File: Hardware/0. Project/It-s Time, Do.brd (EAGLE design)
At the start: 160 x 100 mm, 67 parts, among them CN1 CELL-CONNECTOR, CN13 USB 3.2 Gen 2 Type C Receptac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, CN2 2P-MINI-FIT-JR, CN3 3P-MINI-FIT-JR, CN4 JTAG, CN5 CR-1220, Q1 P-FET-ENHANCEMENT-SI2369BDS, Q14 NPN-BC817, Q15 NPN-BC817, Q3 BC817, U1 MCP73831, U12 CP2102N, U2 TLV75530PDBVR, U3 LMV321, U8 DS3231-SO16

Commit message: Schematic WIP
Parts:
- removed C75, C76: 1nF, My-RLC:C0603
- removed R78: DNP, My-RLC:R0603
- added C11, C12: 1nF, My-RLC:C0603
- R76, R77: value 22R -> 22R (5%)
- R82: value 22k -> 10k (5%)
- R83, R85: value 4k7 -> 4k7 (5%)
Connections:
- net ADC_BATTERY_VOLTAGE renamed ESP32_ADC_BATTERY_SUPPLY_MONITOR
- net GPIO_BATTERY_CHARGING_STATUS renamed ESP32_GPIO_BATTERY_CHARGING_STATUS
- removed net ESP32_GPIO_USB_DETECT: R71.2, R72.1
- removed net ESP32_GPIO_USB_DETECT1: U12.8
- removed net ESP32_PROG_ENABLE: C44.1, C75.1, CN4.10, Q14.3, R86.2, SOC1.3
- removed net ESP32_PROG_MODE: C76.1, Q15.3, R87.2, SOC1.25
- removed net ESP32_SERIAL1_UART_RX: SOC1.27
- removed net ESP32_SERIAL1_UART_TX: SOC1.28
- removed net ESP32_SERIAL2_UART_RX: SOC1.7
- removed net ESP32_SERIAL2_UART_TX: SOC1.9
- removed net ESP32_SERIAL_UART_RX: SOC1.34
- removed net ESP32_SERIAL_UART_TX: SOC1.35
- removed net N$48: R82.1, U12.9
- removed net N$49: R78.2, U12.11
- new net ESP32_GPIO_EXTERNAL_SUPPLY_MONITOR: R71.2, R72.1, U12.8
- new net ESP32_GPIO_PROG_ENABLE: C11.1, C44.1, CN4.10, Q14.3, R86.2, SOC1.3
- new net ESP32_GPIO_PROG_MODE: C12.1, Q15.3, R87.2, SOC1.25
- new net N$17: C72.2, U12.3, U12.EXP, U12.M
- new net N$18: R82.2, U12.9
- net 0V: now also C11.2, C12.2; no longer C72.2, C75.2, C76.2, R78.1, U12.3, U12.EXP, U12.M
- net 3.3V: now also R82.1; no longer R82.2
- net ESP32_UART_RX_USB: now also SOC1.34
- net ESP32_UART_TX_USB: now also SOC1.35
- net ESP32_USB_RTS: now also R85.1; no longer R85.2
- net N$16: now also R85.2; no longer R85.1

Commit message: Schematic WIP
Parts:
- removed C46: 100nF, My-RLC:C0603
- removed Q14: NPN-BC817, My-Transistors:SOT23-3
- removed R71: 24k, My-RLC:R0603
- removed R86, R87: 10k (1%), My-RLC:R0603
- removed U8: DS3231-SO16, My-ICs:SOIC-16W_(SO16)
- added C14: 1nF, My-RLC:C0603
- added C16: 10nF, My-RLC:C0603
- added Q4: BC817, My-Transistors:SOT23-3
- added R14: 47R, My-RLC:R0603
- added R20: 4k7 (5%), My-RLC:R0603
- added R21: 10k (5%), My-RLC:R0603
- added U4: LMV321, My-OpAmps:SOT-23-5
- C10: value 100nF -> 100uF x 10V; device My-RLC:C0603 -> My-RLC:PTH-5MM
- C12: value 1nF -> 100nF
- C2: value 10nF -> 1uF
- C3: value 100nF -> 10uF
- C6: value 10uF -> 100nF
- C7: value 100uF x 10V -> 100nF; device My-RLC:PTH-5MM -> My-RLC:C0603
- C8: value 1uF -> 10uF
- CN1: value CELL-CONNECTOR -> CR-1220; device My-Battery:JST-PH2 -> My-Battery:CR1220/1225_HOLDER
- CN2: value 2P-MINI-FIT-JR -> CELL-CONNECTOR; device My-Connectors:MINI-FIT-JR-2P -> My-Battery:JST-PH2
- CN3: value 3P-MINI-FIT-JR -> JTAG; device My-Connectors:MINI-FIT-JR-3P -> My-Connectors:JTAG-ARM-10P
- CN4: value JTAG -> 2P-MINI-FIT-JR; device My-Connectors:JTAG-ARM-10P -> My-Connectors:MINI-FIT-JR-2P
- CN5: value CR-1220 -> 3P-MINI-FIT-JR; device My-Battery:CR1220/1225_HOLDER -> My-Connectors:MINI-FIT-JR-3P
- Q3: value BC817 -> NPN-BC817
- R1: value 47R -> 10k (5%)
- R11: value 4k7 (5%) -> 24k
- R13: value 10k (5%) -> 22K (5%)
- R15, R16: value 1M -> 10k (1%)
- R2, R3: value 4k7 (5%) -> 10k (5%)
- R5, R6: value 10k (5%) -> 4k7 (5%)
- R7: value 10k (5%) -> 100R (5%)
- R8: value 4k7 -> 1M
- R9: value 100R (5%) -> 1M
- U1: value MCP73831 -> DS3231-SO16; device My-ICs:SOT-23-5 -> My-ICs:SOIC-16W_(SO16)
- U3: value LMV321 -> MCP73831; device My-OpAmps:SOT-23-5 -> My-ICs:SOT-23-5
- moved C4 232.2 mm to (-98.1, -129.9)
- moved R15 221.1 mm to (-77.9, -121.1)
- moved R16 211.3 mm to (-68.7, -113.8)
- moved C12 210.4 mm to (-77.5, 80.0)
- moved R13 154.5 mm to (-22.9, 94.0)
- moved CN3 154.3 mm to (-54.6, 57.1)
- moved CN5 147.0 mm to (-71.9, -96.2)
- moved R11 134.8 mm to (-57.1, 94.0)
- moved Q3 65.0 mm to (-73.2, -106.8)
- moved CN2 58.4 mm to (-43.2, 69.8)
- moved R1 56.2 mm to (-74.9, 87.6)
- moved CN4 47.5 mm to (-41.9, 11.4)
- moved CN1 35.3 mm to (-21.6, 41.9)
- moved U1 34.9 mm to (-44.5, 58.4)
- moved C3 33.0 mm to (-25.4, 88.9)
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- renumbered C44 to C15, C45 to C13, C67 to C20, C69 to C19, C71 to C18, C72 to C21, CN13 to CN6, D7 to D2, Q15 to Q2, R62 to R24, R63 to R23, R65 to R18, R72 to R12, R76 to R25, R77 to R26, R82 to R22, R83 to R19, R85 to R17, U12 to U5
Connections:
- net ESP32_USB_DTR renamed N$20
- removed net N$17: C21.2, U5.3, U5.EXP, U5.M
- removed net N$9: CN5.+, U8.14
- new net RTC_VBAT: C4.1, CN1.+, U1.14
- net !DISPLAY_OLED_RESET: now also R2.1; no longer R5.1
- net 0V: now also C14.2, C16.2, C17.2, C21.2, C7.1, CN1.-, CN3.3, CN3.5, CN3.9, CN4.2, Q4.2, R13.1, R21.2, R3.1, R9.1, U1.10, U1.11, U1.12, U1.13, U1.5, U1.6, U1.7, U1.8, U1.9, U4.2, U5.3, U5.EXP, U5.M; no longer C17.1, C46.2, C7.2, CN1.2, CN4.3, CN4.5, CN4.9, CN5.-, Q3.2, R13.2, R16.1, R7.1, R8.1, U1.2, U8.10, U8.11, U8.12, U8.13, U8.5, U8.6, U8.7, U8.8, U8.9
- net 3.3V: now also C12.1, C17.1, C2.1, C7.2, CN3.1, R1.2, R15.1, R16.1, U1.2, U4.5; no longer C10.1, C17.2, C4.1, C46.1, CN4.1, R3.2, R86.1, R87.1, U3.5, U8.2
- net ESP32_ADC_BATTERY_SUPPLY_MONITOR: now also R8.1, R9.2, SOC1.4; no longer R15.1, R16.2
- net ESP32_ADC_TASK_FEEDBACK_MONITOR: now also C16.1, R14.2; no longer C2.1, R1.2
- net ESP32_GPIO_BATTERY_CHARGING_STATUS: now also SOC1.6, U3.1; no longer U1.1
- net ESP32_GPIO_EXTERNAL_SUPPLY_MONITOR: now also R11.2, SOC1.5; no longer R71.2
- net ESP32_GPIO_PROG_ENABLE: now also C14.1, CN3.10, Q3.3, R16.2; no longer C11.1, CN4.10, Q14.3, R86.2
- net ESP32_GPIO_PROG_MODE: now also C11.1, R15.2; no longer C12.1, R87.2
- net ESP32_GPIO_TASK_CONTROLLER: now also R20.2, R21.1; no longer R11.2, R13.1
- net ESP32_I2C_SCL: now also R5.1, U1.16; no longer R3.1, U8.16
- net ESP32_I2C_SDA: now also R6.1, U1.15; no longer R2.1, U8.15
- net ESP32_USB_RTS: now also Q3.2; no longer Q14.2
- net JTAG_TCK: now also CN3.4; no longer CN4.4
- net JTAG_TDI: now also CN3.8; no longer CN4.8
- net JTAG_TDO: now also CN3.6; no longer CN4.6
- net JTAG_TMS: now also CN3.2; no longer CN4.2
- net N$1: now also C3.1; no longer C5.1
- net N$11: now also R7.2; no longer R9.2
- net N$12: now also R14.1, U4.1, U4.4; no longer R1.1, U3.1, U3.4
- net N$13: now also Q3.1; no longer Q14.1
- net N$14: now also CN5.2; no longer CN3.2
- net N$15: now also CN5.3; no longer CN3.3
- net N$2: now also R1.1; no longer R6.1
- net N$26: now also R13.2, U3.5; no longer R8.2, U1.5
- net N$3: now also R3.2; no longer R7.2
- net N$4: now also CN4.1, U4.3; no longer CN2.1, U3.3
- net N$41: now also Q4.1, R20.1; no longer Q3.1, R11.1
- net N$42: now also Q4.3; no longer Q3.3
- net N$5: now also CN5.1; no longer CN3.1
- net N$7: now also C5.1; no longer C6.1
- net P$1: now also CN2.1, R8.2, U3.3; no longer CN1.1, R15.2, U1.3
- net USB_N: now also CN6.A7, CN6.B7
- net USB_P: now also CN6.A6, CN6.B6
- net VBUS: now also R11.1, R7.1, U3.4; no longer R71.1, R9.1, U1.4
- net VSYS: now also C10.1, C6.1; no longer C3.1, C7.1

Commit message: Schematic WIP
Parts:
- C10: value 100uF x 10V -> 100nF; device My-RLC:PTH-5MM -> My-RLC:C0603
- C12: value 100nF -> 100uF x 10V; device My-RLC:C0603 -> My-RLC:PTH-5MM
- C13, C15, C3, C5: value 10uF -> 100nF
- C14: value 1nF -> 10uF
- C16: value 10nF -> 100nF
- C17, C19, C7, C9: value 100nF -> 10uF
- C2: value 1uF -> 4.7nF
- C20: value 4.7nF -> 1uF
- C6: value 100nF -> 10nF
- C8: value 10uF -> 1nF
- CN1: value CR-1220 -> USB 3.2 Gen 2 Type C Receptacle; device My-Battery:CR1220/1225_HOLDER -> My-Connectors:USB-C-24P
- CN2: value CELL-CONNECTOR -> 3P-MINI-FIT-JR; device My-Battery:JST-PH2 -> My-Connectors:MINI-FIT-JR-3P
- CN3: value JTAG -> 2P-MINI-FIT-JR; device My-Connectors:JTAG-ARM-10P -> My-Connectors:MINI-FIT-JR-2P
- CN4: value 2P-MINI-FIT-JR -> JTAG; device My-Connectors:MINI-FIT-JR-2P -> My-Connectors:JTAG-ARM-10P
- CN5: value 3P-MINI-FIT-JR -> CELL-CONNECTOR; device My-Connectors:MINI-FIT-JR-3P -> My-Battery:JST-PH2
- CN6: value USB 3.2 Gen 2 Type C Receptacle -> CR-1220; device My-Connectors:USB-C-24P -> My-Battery:CR1220/1225_HOLDER
- D1: value SCHOTTKY-SS16 -> FM4004
- D2: value FM4004 -> SCHOTTKY-SS16
- Q1: value P-FET-ENHANCEMENT-SI2369BDS -> BC817
- Q4: value BC817 -> P-FET-ENHANCEMENT-SI2369BDS
- R1, R2: value 10k (5%) -> 22R (5%)
- R10: value 10k (5%) -> 10k (1%)
- R11: value 24k -> 4k7 (5%)
- R12: value 47k -> 10k (1%)
- R13: value 22K (5%) -> 47R
- R14: value 47R -> 22K (5%)
- R15: value 10k (1%) -> 24k
- R16: value 10k (1%) -> 47k
- R17, R5, R6: value 4k7 (5%) -> 10k (5%)
- R18: value 5k1 -> 1M
- R19: value 4k7 (5%) -> 1M
- R20: value 4k7 (5%) -> 100R (5%)
- R21, R22: value 10k (5%) -> 4k7 (5%)
- R23: value 1M -> 390k (1%)
- R24: value 5k1 -> 10k (5%)
- R25, R26: value 22R (5%) -> 10k (5%)
- R3: value 10k (5%) -> 5k1
- R4: value 390k (1%) -> 1M
- R7: value 100R (5%) -> 4k7 (5%)
- R8: value 1M -> 4k7 (5%)
- R9: value 1M -> 5k1
- U1: value DS3231-SO16 -> CP2102N; device My-ICs:SOIC-16W_(SO16) -> My-ICs:QFN-28
- U2: value TLV75530PDBVR -> LMV321; device My-LDOs:SOT-23-5 -> My-OpAmps:SOT-23-5
- U4: value LMV321 -> TLV75530PDBVR; device My-OpAmps:SOT-23-5 -> My-LDOs:SOT-23-5
- U5: value CP2102N -> DS3231-SO16; device My-ICs:QFN-28 -> My-ICs:SOIC-16W_(SO16)
- moved R17 231.8 mm to (-15.2, 94.0)
- moved C18 230.8 mm to (-98.1, -129.9)
- moved C4 230.8 mm to (-41.9, 94.0)
- moved R8 230.2 mm to (-75.6, -131.0)
- moved R19 229.4 mm to (-30.5, 94.0)
- moved C14 228.8 mm to (-20.3, 88.9)
- moved C8 228.8 mm to (-87.3, -129.9)
- moved R11 225.4 mm to (-71.3, -131.0)
- moved R22 219.1 mm to (-64.8, 87.6)
- moved R5 219.1 mm to (-79.9, -131.0)
- moved R15 216.1 mm to (-57.1, 94.0)
- moved R12 215.8 mm to (-77.9, -121.1)
- moved R10 214.6 mm to (-68.7, -113.8)
- moved R25 213.9 mm to (-80.0, 87.6)
- moved R26 213.8 mm to (-74.9, 87.6)
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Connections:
- net !DISPLAY_OLED_RESET: now also R24.1; no longer R2.1
- net 0V: now also C15.1, C18.2, C19.2, C2.1, C20.2, C3.1, C4.1, C7.2, CN1.A1, CN1.A12, CN1.B1, CN1.B12, CN3.2, CN4.3, CN4.5, CN4.9, CN5.2, CN6.-, Q1.2, R14.1, R16.2, R17.1, R19.1, R23.1, R25.1, R3.2, R4.2, R6.2, R9.2, U1.3, U1.EXP, U1.M, U5.10, U5.11, U5.12, U5.13, U5.5, U5.6, U5.7, U5.8, U5.9; no longer C15.2, C18.1, C19.1, C2.2, C20.1, C3.2, C4.2, C7.1, CN1.-, CN2.2, CN3.3, CN3.5, CN3.9, CN4.2, CN6.A1, CN6.A12, CN6.B1, CN6.B12, Q4.2, R10.1, R12.2, R13.1, R18.2, R21.2, R23.2, R24.2, R3.1, R4.1, R9.1, U1.10, U1.11, U1.12, U1.13, U1.5, U1.6, U1.7, U1.8, U1.9, U5.3, U5.EXP, U5.M
- net 3.3V: now also C10.1, C14.1, C15.2, C20.1, C5.1, CN4.1, R10.1, R12.1, R21.2, R22.2, R24.2, R26.2, R5.1, U1.6, U1.7, U5.2; no longer C12.1, C17.1, C2.1, C7.2, C8.1, CN3.1, R1.2, R15.1, R16.1, R2.2, R22.1, R5.2, R6.2, U1.2, U5.6, U5.7
- net ESP32_ADC_BATTERY_SUPPLY_MONITOR: now also R18.1, R19.2; no longer R8.1, R9.2
- net ESP32_ADC_TASK_FEEDBACK_MONITOR: now also C6.1, R13.2, SOC1.11; no longer C16.1, R14.2
- net ESP32_GPIO_EXTERNAL_SUPPLY_MONITOR: now also R15.2, R16.1, U1.8; no longer R11.2, R12.1, U5.8
- net ESP32_GPIO_PROG_ENABLE: now also C7.1, C8.1, CN4.10, Q2.3, R10.2; no longer C14.1, C15.1, CN3.10, Q3.3, R16.2
- net ESP32_GPIO_PROG_MODE: now also Q3.3, R12.2; no longer Q2.3, R15.2
- net ESP32_GPIO_TASK_CONTROLLER: now also R6.1, R7.2, SOC1.8; no longer R20.2, R21.1
- net ESP32_I2C_SCL: now also R22.1, U5.16; no longer R5.1, U1.16
- net ESP32_I2C_SDA: now also R21.1, U5.15; no longer R6.1, U1.15
- net ESP32_UART_RX_USB: now also U1.26; no longer U5.26
- net ESP32_UART_TX_USB: now also U1.25; no longer U5.25
- net ESP32_USB_RTS: now also Q2.2, R11.1, U1.24; no longer Q3.2, R17.1, U5.24
- net JTAG_TCK: now also CN4.4; no longer CN3.4
- net JTAG_TDI: now also CN4.8; no longer CN3.8
- net JTAG_TDO: now also CN4.6; no longer CN3.6
- net JTAG_TMS: now also CN4.2; no longer CN3.2
- net N$1: now also C19.1; no longer C3.1
- net N$10: now also C2.2, CN1.G1, CN1.G2, CN1.G3, CN1.G4, R4.1; no longer C20.2, CN6.G1, CN6.G2, CN6.G3, CN6.G4, R23.1
- net N$11: now also Q4.1, R20.2; no longer Q1.1, R7.2
- net N$12: now also R13.1, U2.1, U2.4; no longer R14.1, U4.1, U4.4
- net N$13: now also Q2.1, R8.1; no longer Q3.1, R19.1
- net N$14: now also CN2.2; no longer CN5.2
- net N$15: now also CN2.3; no longer CN5.3
- net N$16: now also Q3.1, R11.2; no longer Q2.1, R17.2
- net N$18: now also R5.2, U1.9; no longer R22.2, U5.9
- net N$19: now also R1.2, U1.5; no longer R25.2, U5.5
- net N$2: now also R26.1; no longer R1.1
- net N$20: now also Q3.2, R8.2, U1.28; no longer Q2.2, R19.2, U5.28
- net N$21: now also CN1.B5, R9.1; no longer CN6.B5, R18.1
- net N$22: now also R2.2, U1.4; no longer R26.2, U5.4
- net N$26: now also R14.2; no longer R13.2
- net N$3: now also R25.2; no longer R3.2
- net N$4: now also CN3.1, U2.3; no longer CN4.1, U4.3
- net N$41: now also Q1.1, R7.1; no longer Q4.1, R20.1
- net N$42: now also D1.2, Q1.3; no longer D2.2, Q4.3
- net N$5: now also CN2.1; no longer CN5.1
- net N$6: now also R23.2; no longer R4.2
- net N$7: now also C17.1; no longer C5.1
- net N$8: now also CN1.A5, R3.1; no longer CN6.A5, R24.1
- net P$1: now also CN5.1, Q4.3, R18.2; no longer CN2.1, Q1.3, R8.2
- net RTC_VBAT: now also C18.1, CN6.+, U5.14; no longer C4.1, CN1.+, U1.14
- net USB_N: now also CN1.A7, CN1.B7, R1.1; no longer CN6.A7, CN6.B7, R25.1
- net USB_P: now also CN1.A6, CN1.B6, R2.1; no longer CN6.A6, CN6.B6, R26.1
- net VBUS: now also C3.2, C4.2, CN1.A4, CN1.A9, CN1.B4, CN1.B9, D1.1, D2.2, R15.1, R17.2, R20.1; no longer C18.2, C19.2, CN6.A4, CN6.A9, CN6.B4, CN6.B9, D1.2, D2.1, R10.2, R11.1, R7.1
- net VSYS: now also C12.1, C16.1, D2.1, Q4.2, U4.1, U4.3; no longer C10.1, C6.1, D1.1, Q1.2, U2.1, U2.3

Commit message: Schematic v1.0 release
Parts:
- R13: value 47R -> 47R (5%)
- R15: value 24k -> 24k (5%)
- R16: value 47k -> 47k (5%)
- R18, R19, R4: value 1M -> 1M (1%)
- R3, R9: value 5k1 -> 5k1 (1%)
- moved C1 136.6 mm to (-97.5, 12.9)
- moved CN2 136.6 mm to (-98.6, 37.8)
- moved D1 136.6 mm to (-104.1, 90.8)
- moved K1 136.6 mm to (-101.3, 50.5)
- moved Q1 136.6 mm to (-97.8, 92.1)
- moved Q2 136.6 mm to (-99.9, 27.1)
- moved Q3 136.6 mm to (-105.9, 19.1)
- moved R1 136.6 mm to (-97.9, 7.94)
- moved R10 136.6 mm to (-95.4, 20.2)
- moved R11 136.6 mm to (-97.9, 3.02)
- moved R12 136.6 mm to (-104.6, 12.9)
- moved R2 136.6 mm to (-93.7, 7.94)
- moved R5 136.6 mm to (-106.5, 3.02)
- moved R6 136.6 mm to (-106.7, 84.5)
- moved R7 136.6 mm to (-91.4, 93.3)
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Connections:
- net 0V: now also C5.1; no longer C5.2
- net 3.3V: now also C5.2; no longer C5.1

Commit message: Board design WIP
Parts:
- moved C18 224.8 mm to (99.5, 19.1), flipped to the bottom
- moved C11 214.0 mm to (94.1, 19.1), flipped to the bottom
- moved C8 203.3 mm to (88.7, 19.1), flipped to the bottom
- moved R5 188.4 mm to (81.3, 17.9), flipped to the bottom
- moved Q3 187.1 mm to (80.6, 34.0), flipped to the bottom
- moved R12 184.6 mm to (79.4, 27.8), flipped to the bottom
- moved R6 181.2 mm to (74.5, 79.9), flipped to the bottom
- moved R8 179.8 mm to (77.0, 17.9), flipped to the bottom
- moved D1 176.1 mm to (71.9, 86.2), flipped to the bottom
- moved Q2 175.1 mm to (74.6, 42.1), flipped to the bottom
- moved R1 171.3 mm to (72.7, 22.9), flipped to the bottom
- moved R11 171.3 mm to (72.7, 17.9), flipped to the bottom
- moved C1 170.4 mm to (72.2, 27.8), flipped to the bottom
- moved R10 166.2 mm to (70.2, 35.1), flipped to the bottom
- moved Q1 163.4 mm to (65.6, 87.5), flipped to the bottom
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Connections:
- net 0V: now also C2.2, R4.1; no longer C2.1, R4.2
- net N$10: now also C2.1, R4.2; no longer C2.2, R4.1
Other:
- board size 160 x 100 mm -> 50 x 50 mm

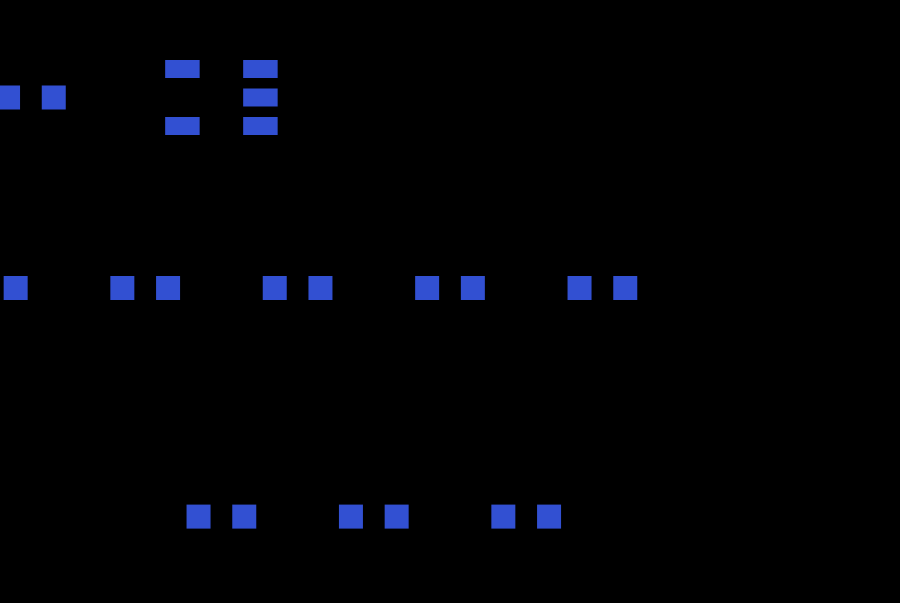
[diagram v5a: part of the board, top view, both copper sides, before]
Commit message: Schematic v1.1 release
- Minor improvements on parts designators position;
- Just one resistor as pull up in not used pins at OLED display.
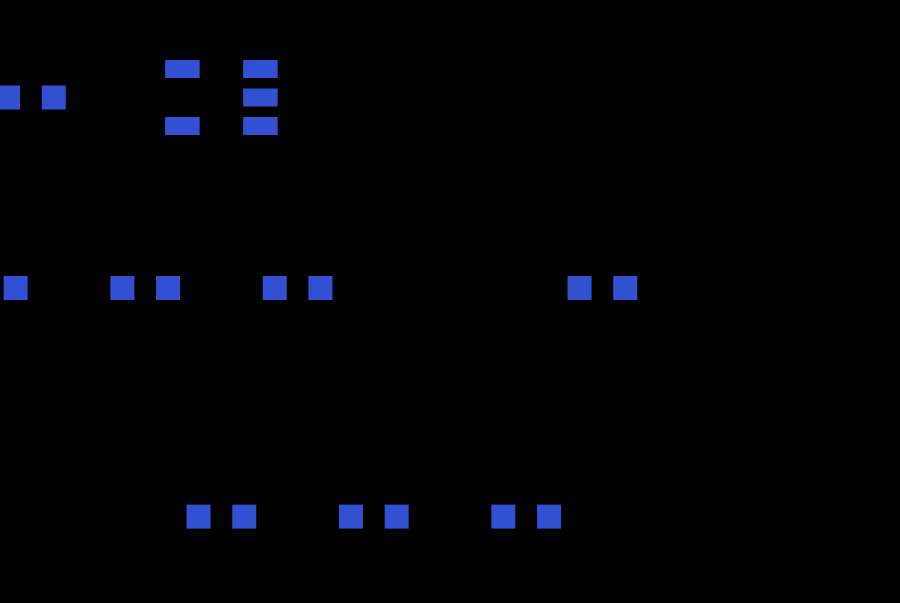
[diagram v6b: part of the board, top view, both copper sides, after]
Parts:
- removed R26: 10k (5%), My-RLC:R0603
- R10, R12: value 10k (1%) -> 10k (5%)
- R4: value 1M (1%) -> 1M (5%)
- R9: value 5k1 (1%) -> 5k1 (5%)
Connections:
- removed net N$2: DS1.15, R26.1
- net !DISPLAY_OLED_RESET: now also DS1.15
- net 3.3V: no longer R26.2

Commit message: Board design WIP
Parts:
- K1: device My-Relays:EC2-5NU -> My-Relays:EE2-5NU
- moved C2 80.7 mm to (19.7, 9.82), flipped to the top, turned to 90 degrees
- moved R12 70.1 mm to (10.3, 15.9), flipped to the top
- moved Q2 70.1 mm to (12.1, 10.5), flipped to the top, turned to 180 degrees
- moved Q3 69.2 mm to (15.6, 10.5), flipped to the top, turned to 180 degrees
- moved C8 61.7 mm to (30.0, 38.1), turned to 90 degrees
- moved R10 57.9 mm to (18.1, 9.81), flipped to the top, turned to 90 degrees
- moved R8 56.0 mm to (21.2, 13.3), flipped to the top, turned to 270 degrees
- moved R11 53.3 mm to (19.6, 13.3), flipped to the top, turned to 270 degrees
- moved C7 52.6 mm to (28.5, 38.1), turned to 90 degrees
- moved R5 51.0 mm to (30.5, 13.1), flipped to the top, turned to 90 degrees
- moved R1 48.6 mm to (25.9, 9.87), flipped to the top, turned to 90 degrees
- moved R2 45.9 mm to (24.4, 9.84), flipped to the top, turned to 90 degrees
- moved C10 45.8 mm to (8.26, 48.3)
- moved C1 45.7 mm to (28.9, 13.0), flipped to the top, turned to 90 degrees
- moved K1 14.9 mm to (29.4, 16.5), turned to 270 degrees
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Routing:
- net JTAG_TMS: track 0.00 -> 25.5 mm
- net N$10: track 0.00 -> 24.7 mm
- net VBUS: track 0.00 -> 20.0 mm
- net JTAG_TDI: track 0.00 -> 19.2 mm, vias 0 -> 2
- net ESP32_USB_RTS: track 0.00 -> 14.0 mm
- net JTAG_TCK: track 0.00 -> 12.9 mm
- net USB_N: track 0.00 -> 12.7 mm, vias 0 -> 2
- net N$21: track 0.00 -> 11.3 mm, vias 0 -> 2
- net 0V: track 0.00 -> 10.1 mm
- net N$20: track 0.00 -> 9.98 mm
- net N$13: track 0.00 -> 9.81 mm
- net JTAG_TDO: track 0.00 -> 7.48 mm
- net 3.3V: track 0.00 -> 6.87 mm
- net ESP32_GPIO_PROG_ENABLE: track 0.00 -> 5.37 mm
- net N$18: track 0.00 -> 4.15 mm
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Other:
- board text added: "C"
- board text added: "INPUT"
- board text added: "NC"
- board text added: "NO"
- board text added: "RELAY OUTPUT"
